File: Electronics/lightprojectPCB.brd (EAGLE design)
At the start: 55.9 x 64.4 mm, 12 parts, among them IC1 7805T

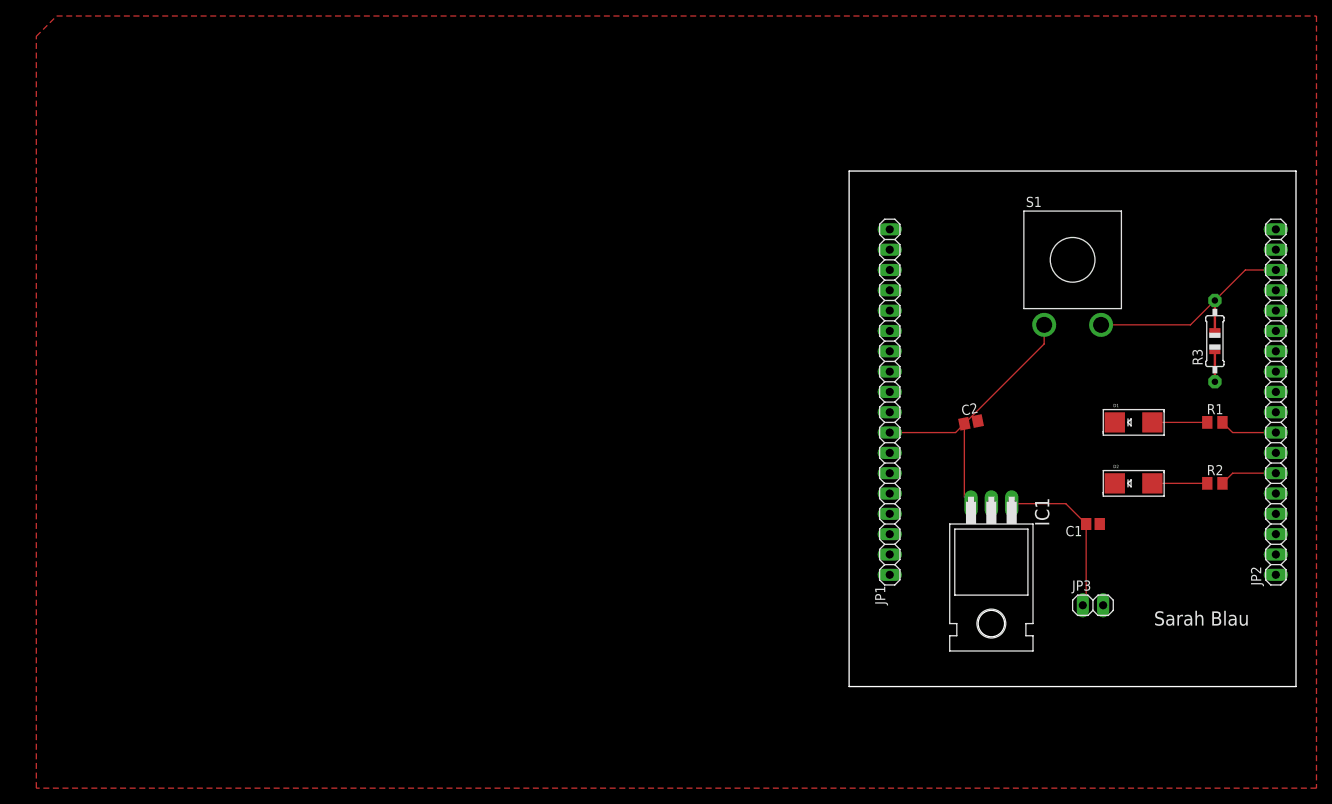
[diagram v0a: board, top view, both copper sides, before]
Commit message: Add files via upload
Updated PCB, but need to redo polygon pour
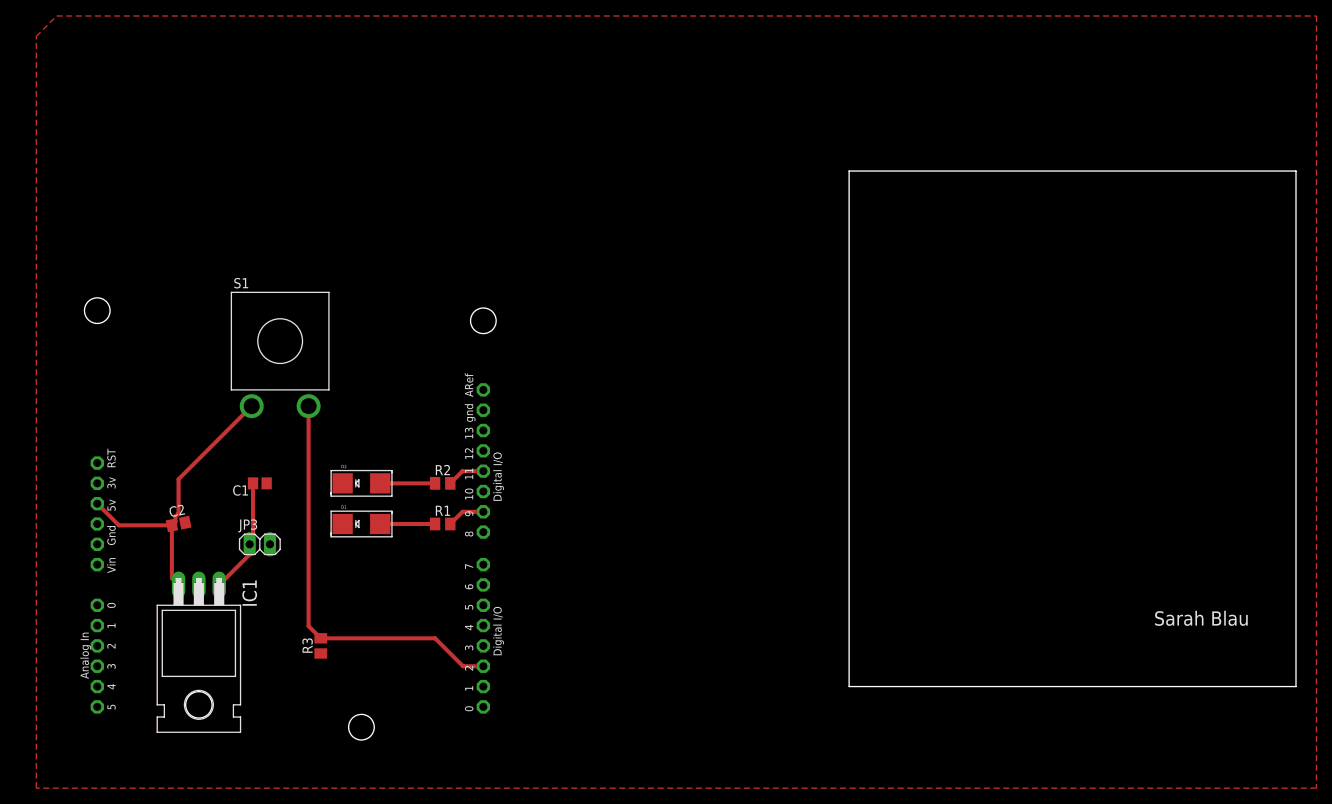
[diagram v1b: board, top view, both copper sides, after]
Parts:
- removed JP1, JP2: (no value), adafruit:1X18
- added U$1: ARDUINO-BPLACE, adafruit:ARDUINO-BPLACE
- R1, R2: value 10kO -> 1kO
- R3: device adafruit:0805-THM -> adafruit:M0805
- moved R3 118.1 mm to (35.6, 20.3)
- moved JP3 104.4 mm to (27.9, 33.0)
- moved C1 104.3 mm to (27.9, 40.6)
- moved C2 99.9 mm to (17.8, 35.6)
- moved IC1 99.6 mm to (20.3, 17.8)
- moved S1 99.6 mm to (30.5, 58.4)
- moved D1 97.4 mm to (40.6, 35.6)
- moved R1 97.4 mm to (50.8, 35.6)
- moved D2 96.5 mm to (40.6, 40.6)
- moved R2 96.5 mm to (50.8, 40.6)
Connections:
- new net 3V: U$1.3V
- new net GND1: U$1.GND1
- new net VIN: U$1.VIN
- net +5V: now also U$1.5V; no longer JP1.8
- net GND: now also U$1.GND, U$1.GND2; no longer JP1.10
- net N$1: now also R1.2, U$1.D9; no longer JP2.16, R3.2, S1.P
- net N$5: now also R3.2, S1.P, U$1.D2; no longer JP2.8, R1.2
- net N$6: now also U$1.D11; no longer JP2.6
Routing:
- net N$5: track 7.20 -> 51.4 mm
- net N$1: track 24.7 -> 4.76 mm
- net N$2: track 20.7 -> 14.5 mm
- net N$6: track 7.20 -> 4.76 mm
- net +5V: track 36.6 -> 37.3 mm

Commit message: Add files via upload
Updated schematic and board to include an analog read of the battery voltage - still need to address polygon pour and make sure there are appropriate components in the lab for my design
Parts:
- moved JP3 20.9 mm to (33.0, 12.7)
- moved C1 15.5 mm to (30.5, 25.4)
- moved R3 8.03 mm to (38.1, 27.9)
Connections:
- net +5V: now also U$1.A1
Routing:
- net +5V: track 37.3 -> 54.9 mm
- net N$2: track 14.5 -> 21.4 mm
- net N$5: track 51.4 -> 45.5 mm
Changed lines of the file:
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@@
 <attribute name="VALUE" x="12.954" y="28.829" size="1.778" layer="27" ratio="10" rot="R270"/>
 </element>
-<element name="C1" library="adafruit" library_urn="urn:adsk.eagle:library:420" package="C0805" package3d_urn="urn:adsk.eagle:package:6240337/1" value="10uF" x="27.94" y="40.64">
-<attribute name="NAME" x="24.511" y="39.116" size="1.27" layer="25"/>
-<attribute name="VALUE" x="27.051" y="38.354" size="1.27" layer="27"/>
+<element name="C1" library="adafruit" library_urn="urn:adsk.eagle:library:420" package="C0805" package3d_urn="urn:adsk.eagle:package:6240337/1" value="10uF" x="30.48" y="25.4">
+<attribute name="NAME" x="27.051" y="23.876" size="1.27" layer="25"/>
+<attribute name="VALUE" x="29.591" y="23.114" size="1.27" layer="27"/>
 </element>
 <element name="C2" library="adafruit" library_urn="urn:adsk.eagle:library:420" package="C0805" package3d_urn="urn:adsk.eagle:package:6240337/1" value="10uF" x="17.78" y="35.56" rot="R11.3">
@@
 <attribute name="VALUE" x="38.1" y="38.354" size="0.4064" layer="27" font="vector"/>
 </element>
-<element name="JP3" library="pinhead" library_urn="urn:adsk.eagle:library:325" package="1X02" package3d_urn="urn:adsk.eagle:package:22435/2" value="" x="27.94" y="33.02">
-<attribute name="NAME" x="25.3238" y="34.8488" size="1.27" layer="25" ratio="10"/>
-<attribute name="VALUE" x="25.4" y="29.845" size="1.27" layer="27"/>
+<element name="JP3" library="pinhead" library_urn="urn:adsk.eagle:library:325" package="1X02" package3d_urn="urn:adsk.eagle:package:22435/2" value="" x="33.02" y="12.7">
+<attribute name="NAME" x="30.4038" y="14.5288" size="1.27" layer="25" ratio="10"/>
+<attribute name="VALUE" x="30.48" y="9.525" size="1.27" layer="27"/>
 </element>
-<element name="R3" library="adafruit" library_urn="urn:adsk.eagle:library:420" package="M0805" package3d_urn="urn:adsk.eagle:package:6240587/1" value="10kO" x="35.56" y="20.32" rot="R90">
-<attribute name="NAME" x="34.544" y="19.304" size="1.27" layer="25" rot="R90"/>
-<attribute name="VALUE" x="37.846" y="19.304" size="1.27" layer="27" rot="R90"/>
+<element name="R3" library="adafruit" library_urn="urn:adsk.eagle:library:420" package="M0805" package3d_urn="urn:adsk.eagle:package:6240587/1" value="10kO" x="38.1" y="27.94" rot="R90">
+<attribute name="NAME" x="37.084" y="26.924" size="1.27" layer="25" rot="R90"/>
+<attribute name="VALUE" x="40.386" y="26.924" size="1.27" layer="27" rot="R90"/>
 </element>
 <element name="U$1" library="adafruit" library_urn="urn:adsk.eagle:library:420" package="ARDUINO-BPLACE" package3d_urn="urn:adsk.eagle:package:6240820/1" value="ARDUINO-BPLACE" x="5.08" y="76.2" rot="R270"/>
@@
 <contactref element="C1" pad="1"/>
 <contactref element="JP3" pad="1"/>
-<wire x1="22.86" y1="27.94" x2="26.67" y2="31.75" width="0.508" layer="1"/>
-<wire x1="26.67" y1="31.75" x2="26.67" y2="33.02" width="0.508" layer="1"/>
-<wire x1="27.09" y1="40.64" x2="27.09" y2="33.44" width="0.508" layer="1"/>
-<wire x1="27.09" y1="33.44" x2="26.67" y2="33.02" width="0.508" layer="1"/>
+<wire x1="31.75" y1="12.7" x2="31.75" y2="19.05" width="0.508" layer="1"/>
+<wire x1="29.63" y1="21.17" x2="29.63" y2="25.4" width="0.508" layer="1"/>
+<wire x1="31.75" y1="19.05" x2="29.63" y2="21.17" width="0.508" layer="1"/>
+<wire x1="29.63" y1="25.4" x2="27.09" y2="27.94" width="0.508" layer="1"/>
+<wire x1="27.09" y1="27.94" x2="22.86" y2="27.94" width="0.508" layer="1"/>
 </signal>
 <signal name="+5V">
@@
 <wire x1="26.924" y1="50.292" x2="17.78" y2="41.148" width="0.508" layer="1"/>
 <wire x1="17.78" y1="41.148" x2="17.78" y2="36.895725" width="0.508" layer="1"/>
-<wire x1="10.32655625" y1="35.39344375" x2="16.946475" y2="35.39344375" width="0.508" layer="1"/>
+<wire x1="10.32655625" y1="35.39344375" x2="12.7" y2="35.39344375" width="0.508" layer="1"/>
+<wire x1="12.7" y1="35.39344375" x2="16.946475" y2="35.39344375" width="0.508" layer="1"/>
 <wire x1="7.62" y1="38.1" x2="10.32655625" y2="35.39344375" width="0.508" layer="1"/>
 <wire x1="16.946475" y1="35.39344375" x2="16.946475" y2="28.773525" width="0.508" layer="1"/>
 <wire x1="16.946475" y1="28.773525" x2="17.78" y2="27.94" width="0.508" layer="1"/>
+<contactref element="U$1" pad="A1"/>
+<wire x1="12.7" y1="35.39344375" x2="12.7" y2="22.86" width="0.508" layer="1"/>
+<wire x1="12.7" y1="22.86" x2="7.62" y2="22.86" width="0.508" layer="1"/>
 </signal>
 <signal name="N$3">
@@
 <contactref element="R3" pad="2"/>
 <contactref element="U$1" pad="D2"/>
-<wire x1="34.036" y1="50.292" x2="34.036" y2="22.794" width="0.508" layer="1"/>
-<wire x1="34.036" y1="22.794" x2="35.56" y2="21.27" width="0.508" layer="1"/>
-<wire x1="35.56" y1="21.27" x2="49.85" y2="21.27" width="0.508" layer="1"/>
-<wire x1="49.85" y1="21.27" x2="53.34" y2="17.78" width="0.508" layer="1"/>
+<wire x1="34.036" y1="50.292" x2="34.036" y2="32.954" width="0.508" layer="1"/>
+<wire x1="38.1" y1="28.89" x2="34.036" y2="32.954" width="0.508" layer="1"/>
+<wire x1="42.23" y1="28.89" x2="38.1" y2="28.89" width="0.508" layer="1"/>
+<wire x1="42.23" y1="28.89" x2="53.34" y2="17.78" width="0.508" layer="1"/>
 <wire x1="53.34" y1="17.78" x2="55.88" y2="17.78" width="0.508" layer="1"/>
 </signal>

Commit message: Add files via upload
Moved board back to origin, should be finalized
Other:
- board size 55.9 x 64.4 mm -> 63.5 x 82.2 mm
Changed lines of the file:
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@@
 <board>
 <plain>
-<wire x1="101.6" y1="15.24" x2="157.46" y2="15.24" width="0" layer="20"/>
-<wire x1="157.46" y1="15.24" x2="157.46" y2="79.68" width="0" layer="20"/>
-<wire x1="157.46" y1="79.68" x2="101.6" y2="79.68" width="0" layer="20"/>
-<wire x1="101.6" y1="79.68" x2="101.6" y2="15.24" width="0" layer="20"/>
-<text x="139.7" y="22.86" size="1.778" layer="112">Sarah Blau</text>
+<wire x1="0" y1="2.54" x2="63.48" y2="2.54" width="0" layer="20"/>
+<wire x1="63.48" y1="2.54" x2="63.48" y2="84.76" width="0" layer="20"/>
+<wire x1="63.48" y1="84.76" x2="0" y2="84.76" width="0" layer="20"/>
+<wire x1="0" y1="84.76" x2="0" y2="2.54" width="0" layer="20"/>
+<text x="45.72" y="50.8" size="1.778" layer="112" rot="R90">Sarah Blau</text>
 </plain>
 <attributes>
@@
 <polygon width="0.1524" layer="1">
 <vertex x="2.54" y="99.06"/>
-<vertex x="160.02" y="99.06"/>
-<vertex x="160.02" y="2.54"/>
-<vertex x="0" y="2.54"/>
-<vertex x="0" y="96.52"/>
+<vertex x="157.48" y="99.06"/>
+<vertex x="157.48" y="2.54"/>
+<vertex x="-2.54" y="2.54"/>
+<vertex x="-2.54" y="93.98"/>
 </polygon>
 <contactref element="R3" pad="1"/>

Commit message: Add files via upload
Shortened the board so it wouldn't hang over the Arduino on the edge where I need the ports to be accessible
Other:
- board size 63.5 x 82.2 mm -> 63.5 x 72.1 mm
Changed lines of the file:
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@@
 <plain>
 <wire x1="0" y1="2.54" x2="63.48" y2="2.54" width="0" layer="20"/>
-<wire x1="63.48" y1="2.54" x2="63.48" y2="84.76" width="0" layer="20"/>
-<wire x1="63.48" y1="84.76" x2="0" y2="84.76" width="0" layer="20"/>
-<wire x1="0" y1="84.76" x2="0" y2="2.54" width="0" layer="20"/>
+<wire x1="63.48" y1="2.54" x2="63.48" y2="74.6" width="0" layer="20"/>
+<wire x1="63.48" y1="74.6" x2="0" y2="74.6" width="0" layer="20"/>
+<wire x1="0" y1="74.6" x2="0" y2="2.54" width="0" layer="20"/>
 <text x="45.72" y="50.8" size="1.778" layer="112" rot="R90">Sarah Blau</text>
 </plain>
